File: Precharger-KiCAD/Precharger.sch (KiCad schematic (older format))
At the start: 18 parts

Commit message: Making a start on the PCB
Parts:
- removed J? (x2): Anderson_PP45_Power_RA, Anderson_Powerpole:Anderson_Powerpole-45A-RA-Bottom-Pair, symbol Anderson_Powerpole:Anderson_PP45_Power_RA
- added C4: 10uF, Capacitor_SMD:C_0805_2012Metric_Pad1.15x1.40mm_HandSolder, symbol Device:C
- added C5: 100nF, Capacitor_SMD:C_0805_2012Metric_Pad1.15x1.40mm_HandSolder, symbol Device:C
- added J1: Connector_Screw_Terminal_01x05, Connector_Phoenix_MC:PhoenixContact_MCV_1,5_5-G-3.5_1x05_P3.50mm_Vertical, symbol Breakout_Board:Connector_Screw_Terminal_01x05
- added J2, J3: Anderson_PP45_Power_RA, Anderson_Powerpole:Anderson_Powerpole-45A-RA-Bottom-Pair, symbol Anderson_Powerpole:Anderson_PP45_Power_RA
- added JP1, JP2: SolderJumper_2_Open, Jumper:SolderJumper-2_P1.3mm_Open_RoundedPad1.0x1.5mm, symbol Jumper:SolderJumper_2_Open
- added JP3, JP4, JP5, JP6, JP7, JP8: SolderJumper_2_Bridged, Jumper:SolderJumper-2_P1.3mm_Bridged2Bar_RoundedPad1.0x1.5mm, symbol Jumper:SolderJumper_2_Bridged
- added M1, M2: Anderson_PP45_Staple_Nx2, Anderson_Powerpole:Anderson_Powerpole-staple-Nx2, symbol Anderson_Powerpole:Anderson_PP45_Staple_Nx2
- added Q1: SQJQ480E, Precharger:Vishay_PowerPAK_8x8L_Single, symbol Precharger_Lib:SQJQ480E
- added R10, R9: 330R, Resistor_SMD:R_0805_2012Metric_Pad1.15x1.40mm_HandSolder, symbol Device:R
- added R7, R8: 470R 5W, Resistor_THT:R_Axial_Power_L25.0mm_W9.0mm_P30.48mm, symbol Device:R
- added TP1, TP2, TP3, TP4: TestPoint, TestPoint:TestPoint_Keystone_5010-5014_Multipurpose, symbol Connector:TestPoint
- added U4: CPC1004N, Precharger:SOP-4_3.8x4.1mm_P2.54mm_CPC1004N, symbol Precharger_Lib:CPC1004N
- added U5: VOM1271, Precharger:SOP-4_4.57x4.92mm_P2.54mm_VOM1271, symbol Precharger_Lib:VOM1271
- gave numbers to parts that had none: 16
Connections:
- net labels added: EXT_RX, EXT_TX, ~CLOSE, ~PRECHARGE
- wire segments 21 -> 54
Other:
- note added: "If = (5-1.4)/330 -> 11mA"
- moved on the sheet: A1, U6

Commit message: Continuing
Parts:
- removed J1: Connector_Screw_Terminal_01x05, Connector_Phoenix_MC:PhoenixContact_MCV_1,5_5-G-3.5_1x05_P3.50mm_Vertical, symbol Breakout_Board:Connector_Screw_Terminal_01x05
- added C6: 100nF, Capacitor_SMD:C_0805_2012Metric_Pad1.15x1.40mm_HandSolder, symbol Device:C
- added D1: ASMB-MTB1-0A3A2, LED_SMD:LED_Avago_PLCC4_3.2x2.8mm_CW, symbol LED:ASMB-MTB1-0A3A2
- added J1: Screw_Terminal_01x04, TerminalBlock_Phoenix:TerminalBlock_Phoenix_PT-1,5-4-3.5-H_1x04_P3.50mm_Horizontal, symbol Connector:Screw_Terminal_01x04
- added R11: 150R, Resistor_SMD:R_0805_2012Metric_Pad1.15x1.40mm_HandSolder, symbol Device:R
- added R12, R13: 100R, Resistor_SMD:R_0805_2012Metric_Pad1.15x1.40mm_HandSolder, symbol Device:R
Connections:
- net labels added: ISO_GND, ISO_RX, ISO_TX, ISO_VCC, LED_B, LED_G, LED_R
- wire segments 54 -> 74
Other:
- moved on the sheet: A1, C4, C5, R7, R8, TP3, TP4, U6

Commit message: Close to finishing up schematic
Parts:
- added C7: 22uF, Capacitor_THT:CP_Radial_D10.0mm_P5.00mm, symbol Device:C
- added F2: Fuse, General_Library:Fuseholder_Clip-5x20mm_Schurter_0751_0052_Horizontal_Open, symbol Device:Fuse
- added J5: Anderson_PP45_Power_RA, Anderson_Powerpole:Anderson_Powerpole-45A-RA-Bottom-Pair, symbol Anderson_Powerpole:Anderson_PP45_Power_RA
- added JP10, JP9: SolderJumper_2_Bridged, Jumper:SolderJumper-2_P1.3mm_Bridged2Bar_RoundedPad1.0x1.5mm, symbol Jumper:SolderJumper_2_Bridged
- added M3: Anderson_PP45_Staple_Nx2, Anderson_Powerpole:Anderson_Powerpole-staple-Nx2, symbol Anderson_Powerpole:Anderson_PP45_Staple_Nx2
- added PS1: Delta_E48SC12010NRFA, General_Library:Converter_DCDC_Delta_E48SC12010_THT, symbol General_Library:Delta_E48SC12010NRFA
- added Q2: BSS123, Package_TO_SOT_SMD:SOT-23, symbol Transistor_FET:BSS123
- added R14, R15: TRIM_UP, Resistor_SMD:R_0805_2012Metric_Pad1.15x1.40mm_HandSolder, symbol Device:R
- added TP5, TP6, TP7, TP8: TestPoint, TestPoint:TestPoint_Keystone_5010-5014_Multipurpose, symbol Connector:TestPoint
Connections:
- net labels added: AUX_12V_ENA, AUX_12V_NEG, AUX_12V_POS, AUX_SW
- wire segments 74 -> 112

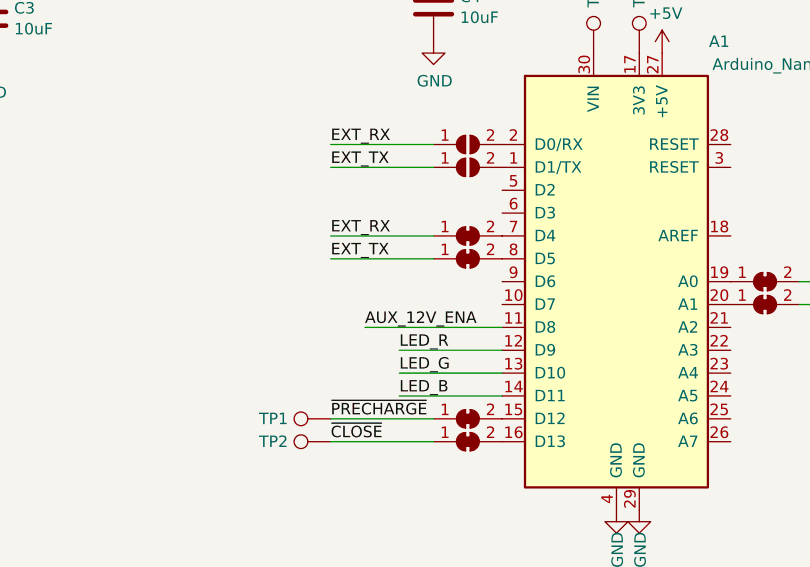
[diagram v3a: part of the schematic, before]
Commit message: Finished routing and generated fab outputs
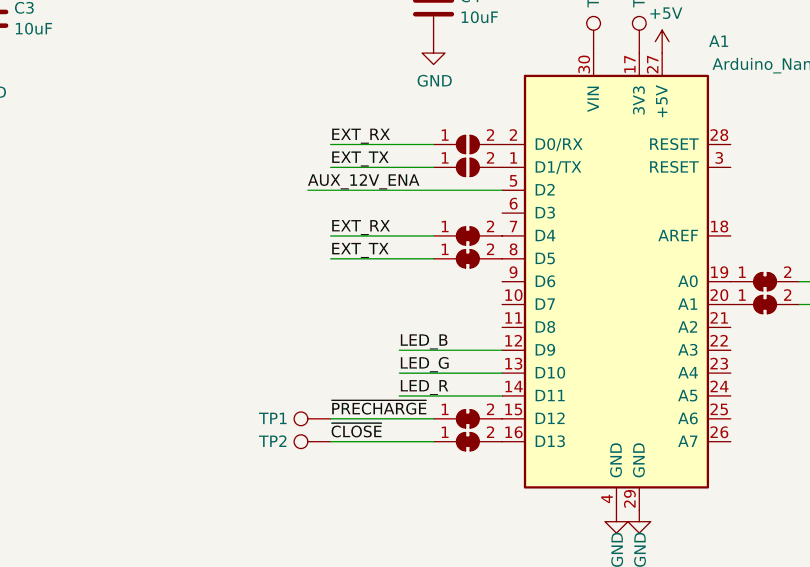
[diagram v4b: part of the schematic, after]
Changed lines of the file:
@@
 Wire Wire Line
 	6300 4550 5850 4550
-Text Label 5850 4550 0    50   ~ 0
+Text Label 5850 4750 0    50   ~ 0
 LED_R
 Wire Wire Line
@@
 Wire Wire Line
 	6300 4750 5850 4750
-Text Label 5850 4750 0    50   ~ 0
+Text Label 5850 4550 0    50   ~ 0
 LED_B
 $Comp
@@
 Wire Wire Line
 	3700 6600 4250 6600
-Text Label 5700 4450 0    50   ~ 0
+Text Label 5450 3850 0    50   ~ 0
 AUX_12V_ENA
-Wire Wire Line
-	5700 4450 6300 4450
 Text Label 2800 7100 0    50   ~ 0
 AUX_12V_ENA
@@
 	0    1    1    0
 $EndComp
+Wire Wire Line
+	5450 3850 6300 3850
 $EndSCHEMATC

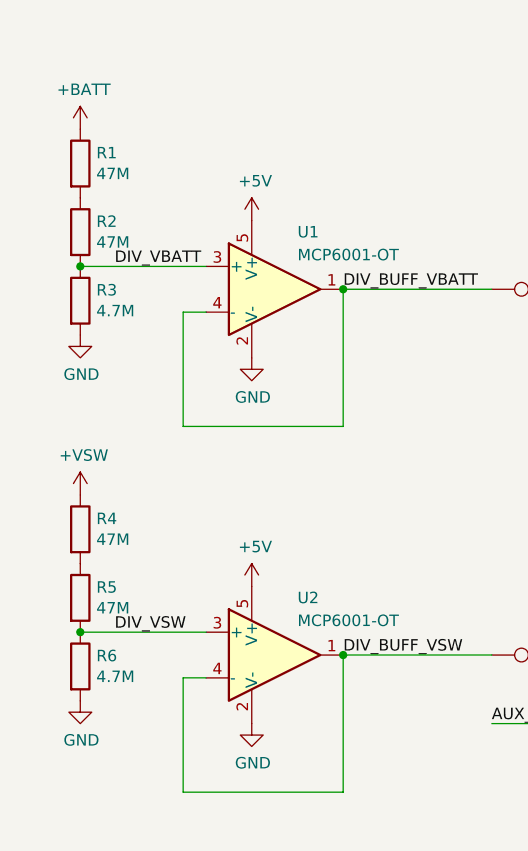
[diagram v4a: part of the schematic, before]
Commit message: Changing dividing resistors down due to reasonably cheap values in 1% tolerence and adding BOM excel file for Digikey Ordering
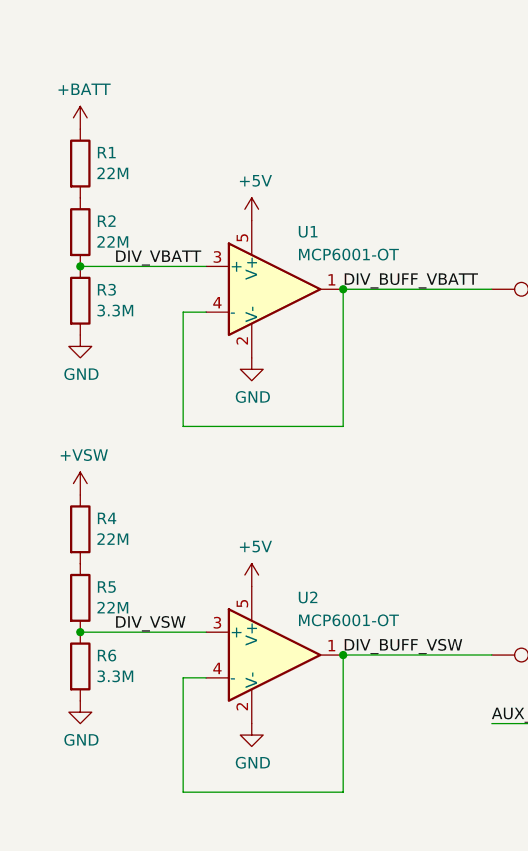
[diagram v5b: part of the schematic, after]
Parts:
- R1, R2, R4, R5: value 47M -> 22M
- R3, R6: value 4.7M -> 3.3M
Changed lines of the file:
@@
 P 1000 5250
 F 0 "R3" H 1070 5296 50  0000 L CNN
-F 1 "4.7M" H 1070 5205 50  0000 L CNN
+F 1 "3.3M" H 1070 5205 50  0000 L CNN
 F 2 "Resistor_SMD:R_0805_2012Metric_Pad1.15x1.40mm_HandSolder" V 930 5250 50  0001 C CNN
 F 3 "~" H 1000 5250 50  0001 C CNN
@@
 P 1000 4950
 F 0 "R2" H 1070 4996 50  0000 L CNN
-F 1 "47M" H 1070 4905 50  0000 L CNN
+F 1 "22M" H 1070 4905 50  0000 L CNN
 F 2 "Resistor_SMD:R_0805_2012Metric_Pad1.15x1.40mm_HandSolder" V 930 4950 50  0001 C CNN
 F 3 "~" H 1000 4950 50  0001 C CNN
@@
 P 1000 4650
 F 0 "R1" H 1070 4696 50  0000 L CNN
-F 1 "47M" H 1070 4605 50  0000 L CNN
+F 1 "22M" H 1070 4605 50  0000 L CNN
 F 2 "Resistor_SMD:R_0805_2012Metric_Pad1.15x1.40mm_HandSolder" V 930 4650 50  0001 C CNN
 F 3 "~" H 1000 4650 50  0001 C CNN
@@
 P 1000 6850
 F 0 "R6" H 1070 6896 50  0000 L CNN
-F 1 "4.7M" H 1070 6805 50  0000 L CNN
+F 1 "3.3M" H 1070 6805 50  0000 L CNN
 F 2 "Resistor_SMD:R_0805_2012Metric_Pad1.15x1.40mm_HandSolder" V 930 6850 50  0001 C CNN
 F 3 "~" H 1000 6850 50  0001 C CNN
@@
 P 1000 6550
 F 0 "R5" H 1070 6596 50  0000 L CNN
-F 1 "47M" H 1070 6505 50  0000 L CNN
+F 1 "22M" H 1070 6505 50  0000 L CNN
 F 2 "Resistor_SMD:R_0805_2012Metric_Pad1.15x1.40mm_HandSolder" V 930 6550 50  0001 C CNN
 F 3 "~" H 1000 6550 50  0001 C CNN
@@
 P 1000 6250
 F 0 "R4" H 1070 6296 50  0000 L CNN
-F 1 "47M" H 1070 6205 50  0000 L CNN
+F 1 "22M" H 1070 6205 50  0000 L CNN
 F 2 "Resistor_SMD:R_0805_2012Metric_Pad1.15x1.40mm_HandSolder" V 930 6250 50  0001 C CNN
 F 3 "~" H 1000 6250 50  0001 C CNN

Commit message: Updating errors
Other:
- note added: "FOOTPRINT ERROR!"
- note added: "Only blocks in one direction! Update SCH symbol"
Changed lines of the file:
@@
 Wire Wire Line
 	5450 3850 6300 3850
+Text Notes 3100 2700 0    50   ~ 0
+FOOTPRINT ERROR!
+Text Notes 4350 850  0    50   ~ 0
+Only blocks in one direction! Update SCH symbol
 $EndSCHEMATC

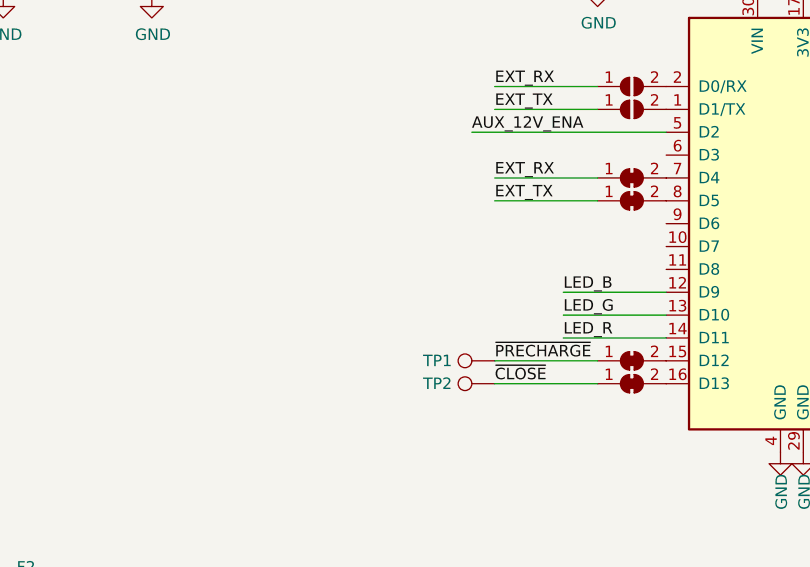
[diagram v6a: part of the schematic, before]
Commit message: Working on arduino code
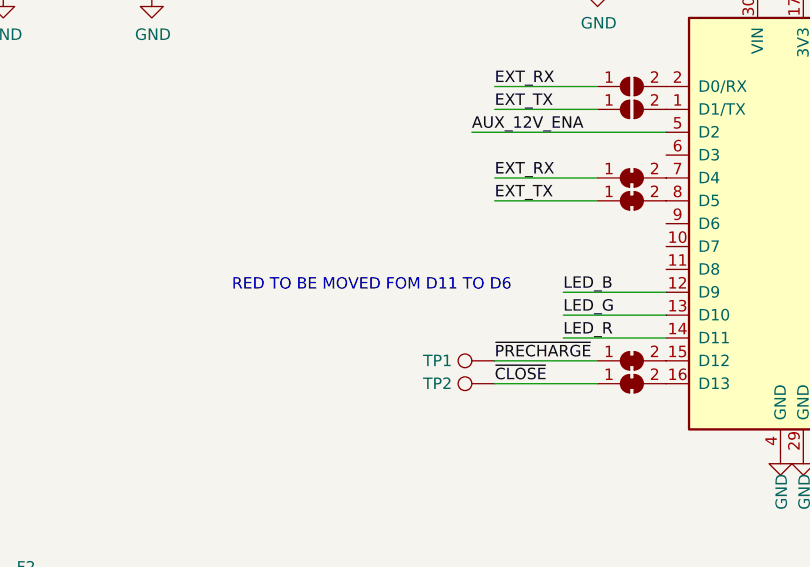
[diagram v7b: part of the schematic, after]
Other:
- note added: "RED TO BE MOVED FOM D11 TO D6"
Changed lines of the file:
@@
 Text Notes 4350 850  0    50   ~ 0
 Only blocks in one direction! Update SCH symbol
+Text Notes 4400 4550 0    50   ~ 0
+RED TO BE MOVED FOM D11 TO D6
 $EndSCHEMATC
